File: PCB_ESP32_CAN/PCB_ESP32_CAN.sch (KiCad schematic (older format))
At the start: 1 part

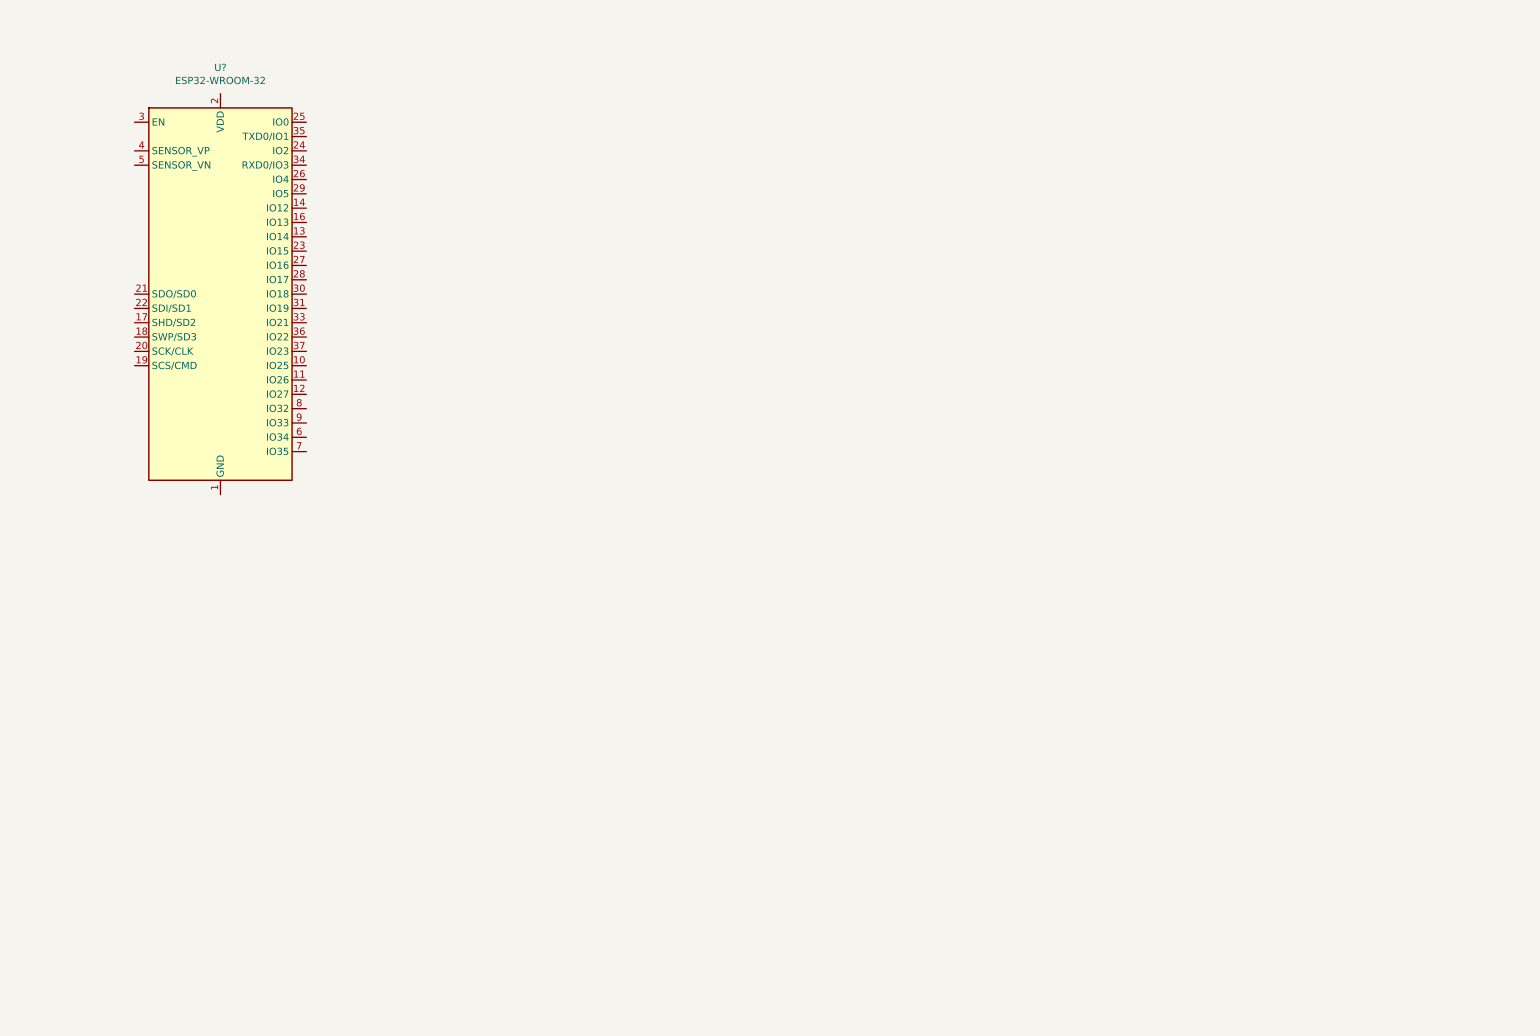
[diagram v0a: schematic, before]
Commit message: esp32 pas fini + silkscreen  IO ok
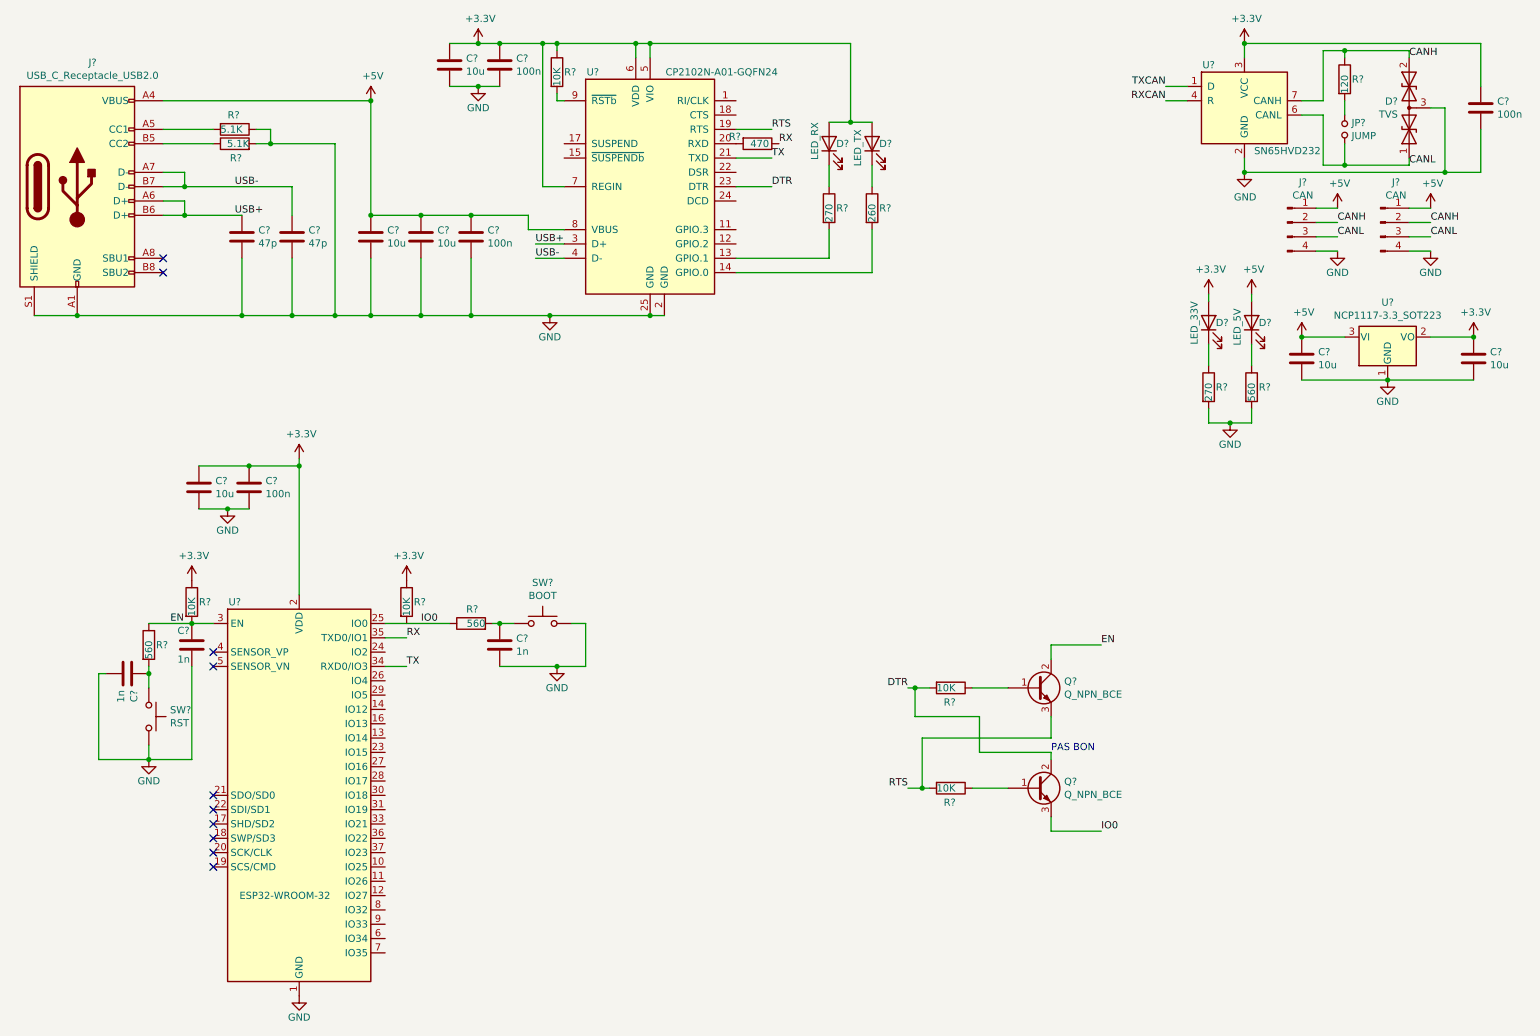
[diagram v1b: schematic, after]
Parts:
- added C? (x4): 100n, symbol Device:C
- added C? (x6): 10u, symbol Device:C
- added C? (x2): 47p, symbol Device:C
- added C? (x3): 1n, symbol Device:C
- added D?: TVS, symbol Device:D_TVS_x2_AAC
- added D?: LED_33V, symbol Device:LED
- added D?: LED_5V, symbol Device:LED
- added D?: LED_RX, symbol Device:LED
- added D?: LED_TX, symbol Device:LED
- added J? (x2): CAN, symbol Connector:Conn_01x04_Male
- added J?: USB_C_Receptacle_USB2.0, symbol Connector:USB_C_Receptacle_USB2.0
- added JP?: JUMP, symbol Device:Jumper_NO_Small
- added Q? (x2): Q_NPN_BCE, symbol Device:Q_NPN_BCE
- added R?: 120, symbol Device:R
- added R? (x3): 560, symbol Device:R
- added R? (x2): 270, symbol Device:R
- added R? (x2): 5.1K, symbol Device:R
- added R?: 260, symbol Device:R
- added R? (x5): 10K, symbol Device:R
- added R?: 470, symbol Device:R
- added SW?: BOOT, symbol Switch:SW_Push
- added SW?: RST, symbol Switch:SW_Push
- added U?: SN65HVD232, Package_SO:SOIC-8_3.9x4.9mm_P1.27mm, symbol Interface_CAN_LIN:SN65HVD232
- added U?: NCP1117-3.3_SOT223, Package_TO_SOT_SMD:SOT-223-3_TabPin2, symbol Regulator_Linear:NCP1117-3.3_SOT223
- added U?: CP2102N-A01-GQFN24, Package_DFN_QFN:QFN-24-1EP_4x4mm_P0.5mm_EP2.6x2.6mm, symbol Interface_USB:CP2102N-A01-GQFN24
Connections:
- net GND: now reaches U?.1 (GND), U?.15 (GND), U?.38 (GND), U?.39 (GND)
- net GND: now also C?.1, C?.2, C?.2, C?.2, C?.2, C?.2, C?.2, C?.2, C?.2, C?.2, C?.2, C?.2, C?.2, C?.2, C?.2, D?.3 (common), J?.4 (Pin_4), J?.4 (Pin_4), J?.A1 (GND), J?.A12 (GND), J?.B1 (GND), J?.B12 (GND), J?.S1 (SHIELD), R?.1, R?.2, R?.2, R?.2, SW?.2, SW?.2, U?.1 (GND), U?.2 (GND), U?.2 (GND), U?.25 (GND)
- net +3V3: now reaches U?.2 (VDD)
- net +3V3: now also C?.1, C?.1, C?.1, C?.1, C?.1, C?.1, D?.2 (A), D?.2 (A), D?.2 (A), R?.1, R?.1, R?.1, U?.2 (VO), U?.3 (VCC), U?.5 (VIO), U?.6 (VDD), U?.7 (REGIN)
- net IO0: now reaches U?.25 (IO0)
- net IO0: now also Q?.3 (E), R?.1
- net EN: now reaches U?.3 (EN)
- net EN: now also C?.2, Q?.2 (C), R?.1, R?.2
- net TX: now reaches U?.34 (RXD0/IO3)
- net TX: now also U?.21 (TXD)
- net RX: now reaches U?.35 (TXD0/IO1)
- net RX: now also R?.1
- new net: JP?.1, R?.2
- new net: D?.1 (K), R?.1 (x4)
- new net: J?.A5 (CC1), R?.2
- new net: J?.B5 (CC2), R?.1
- new net: R?.2, U?.13 (GPIO.1)
- new net: R?.2, U?.14 (GPIO.0)
- new net: R?.2, U?.20 (RXD)
- new net: R?.2, U?.9 (~RSTb)
- new net: Q?.1 (B), R?.1 (x2)
- new net: C?.1, R?.2, SW?.1 (x2)
- new net +5V: C?.1, C?.1, C?.1, C?.1, D?.2 (A), J?.1 (Pin_1), J?.1 (Pin_1), J?.A4 (VBUS), J?.A9 (VBUS), J?.B4 (VBUS), J?.B9 (VBUS), U?.3 (VI), U?.8 (VBUS)
- new net CANH: D?.2 (A2), J?.2 (Pin_2), J?.2 (Pin_2), R?.1, U?.7 (CANH)
- new net CANL: D?.1 (A1), J?.3 (Pin_3), J?.3 (Pin_3), JP?.2, U?.6 (CANL)
- new net DTR: Q?.2 (C), R?.2, U?.23 (DTR)
- new net RTS: Q?.3 (E), R?.2, U?.19 (RTS)
- new net RXCAN: U?.4 (R)
- new net TXCAN: U?.1 (D)
- new net USB+: C?.1, J?.A6 (D+), J?.B6 (D+), U?.3 (D+)
- new net USB-: C?.1, J?.A7 (D-), J?.B7 (D-), U?.4 (D-)
- no-connect marks 0 -> 10
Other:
- note added: "PAS BON"
- moved on the sheet: U?

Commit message: ESP32 fini
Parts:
- added H1, H2, H3, H4: M, MountingHole:MountingHole_3.2mm_M3_Pad_Via, symbol Mechanical:MountingHole_Pad
- added J2, J3: CAN, AREA_lib_Connector:690367290476, symbol Connector:Conn_01x04_Male
- C1, C10, C11, C12, C13, C14, C15, C2, C3, C4, C5, C6, C7, C8, C9: renamed from C?; footprint (none) -> Capacitor_SMD:C_0805_2012Metric_Pad1.18x1.45mm_HandSolder
- D1, D2, D3, D4: renamed from D?; footprint (none) -> LED_SMD:LED_0805_2012Metric_Pad1.15x1.40mm_HandSolder
- D5: renamed from D?; footprint (none) -> Package_TO_SOT_SMD:SOT-23
- J1: renamed from J?; footprint (none) -> Connector_USB:USB_C_Receptacle_GCT_USB4085
- J4, J5: renamed from J?; footprint (none) -> AREA_lib_Connector:Wuerth_2mm_4pin_62000411622
- JP1: renamed from JP?; footprint (none) -> Connector_PinHeader_2.54mm:PinHeader_1x02_P2.54mm_Vertical
- Q1, Q2: renamed from Q?; footprint (none) -> Package_TO_SOT_SMD:SOT-23
- R1, R10, R11, R12, R13, R14, R15, R2, R3, R4, R5, R6, R7, R8, R9: renamed from R?; footprint (none) -> Resistor_SMD:R_0805_2012Metric_Pad1.20x1.40mm_HandSolder
- SW1, SW2: renamed from SW?; footprint (none) -> Button_Switch_SMD:SW_SPST_FSMSM
- gave numbers to parts that had none: 4
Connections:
- net +5V: now also J2.1 (Pin_1), J3.1 (Pin_1)
- net CANH: now also J2.2 (Pin_2), J3.2 (Pin_2)
- net CANL: now also J2.3 (Pin_3), J3.3 (Pin_3)
- net DTR: now also Q2.3 (E); no longer Q2.2 (C)
- net GND: now also H1.1, H2.1, H3.1, H4.1, J2.4 (Pin_4), J3.4 (Pin_4)
- net IO0: now also Q2.2 (C), R5.2; no longer Q2.3 (E)
- net RXCAN: now also U1.26 (IO4)
- net TXCAN: now also U1.29 (IO5)
